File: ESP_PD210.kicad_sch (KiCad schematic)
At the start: 66 parts, among them J1 TTL, J2 CART, J3 USB_C_Receptacle_USB2.0, Q1 NPN, Q2 SE30P09D, SW1 Rocker, SW2 Move, U1 SSD1316, U2 ESP8684, U3 AD8628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

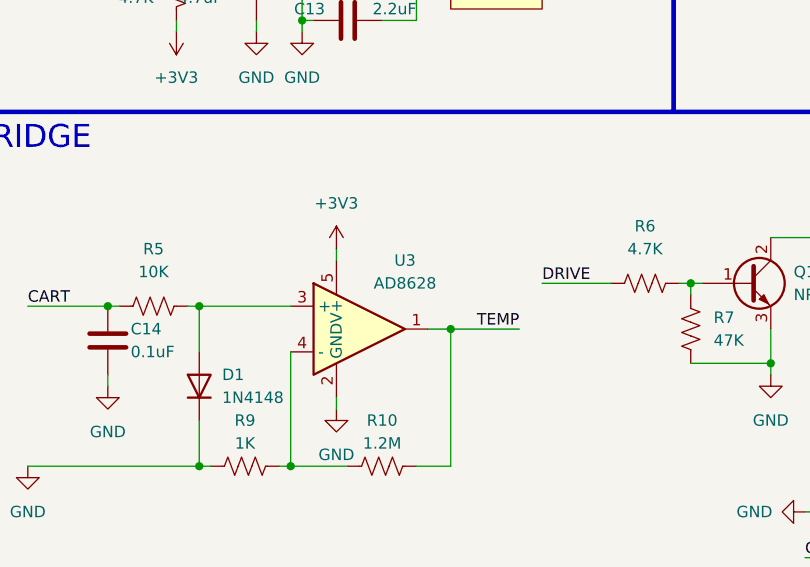
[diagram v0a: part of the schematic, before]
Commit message: Replace the OPA with OPA188
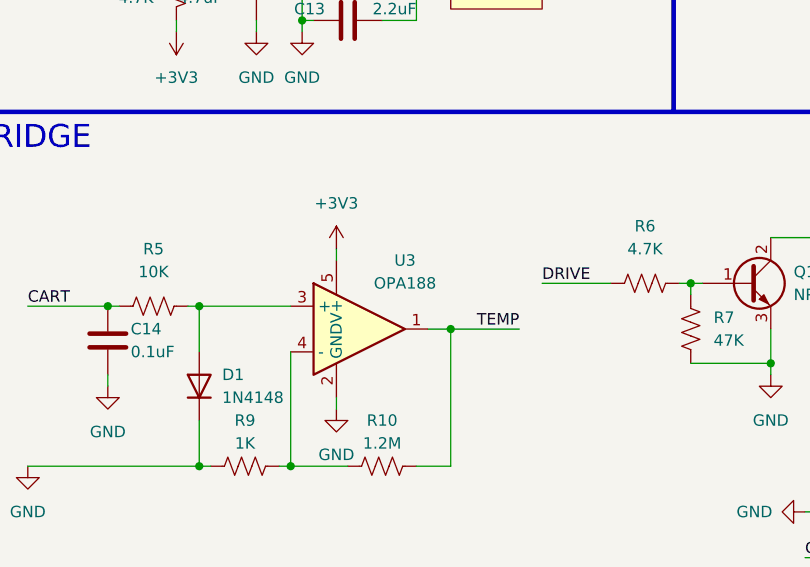
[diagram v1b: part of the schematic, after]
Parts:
- U3: value AD8628 -> OPA188
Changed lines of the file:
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@@
     (in_bom yes) (on_board yes)
     (property "Reference" "U3" (id 0) (at 193.04 82.55 0))
-    (property "Value" "AD8628" (id 1) (at 193.04 85.09 0))
+    (property "Value" "OPA188" (id 1) (at 193.04 85.09 0))
     (property "Footprint" "Package_TO_SOT_SMD:SOT-23-5" (id 2) (at 186.69 86.36 0)
       (effects (font (size 1.27 1.27)) hide)
@@
     )
     (path "/d2aeacdf-d9b9-4b18-ae2f-946cbfd5b011"
-      (reference "U3") (unit 1) (value "AD8628") (footprint "Package_TO_SOT_SMD:SOT-23-5")
+      (reference "U3") (unit 1) (value "OPA188") (footprint "Package_TO_SOT_SMD:SOT-23-5")
     )
     (path "/dade225f-9c7e-4650-bb58-a3ad4a9eac4c"

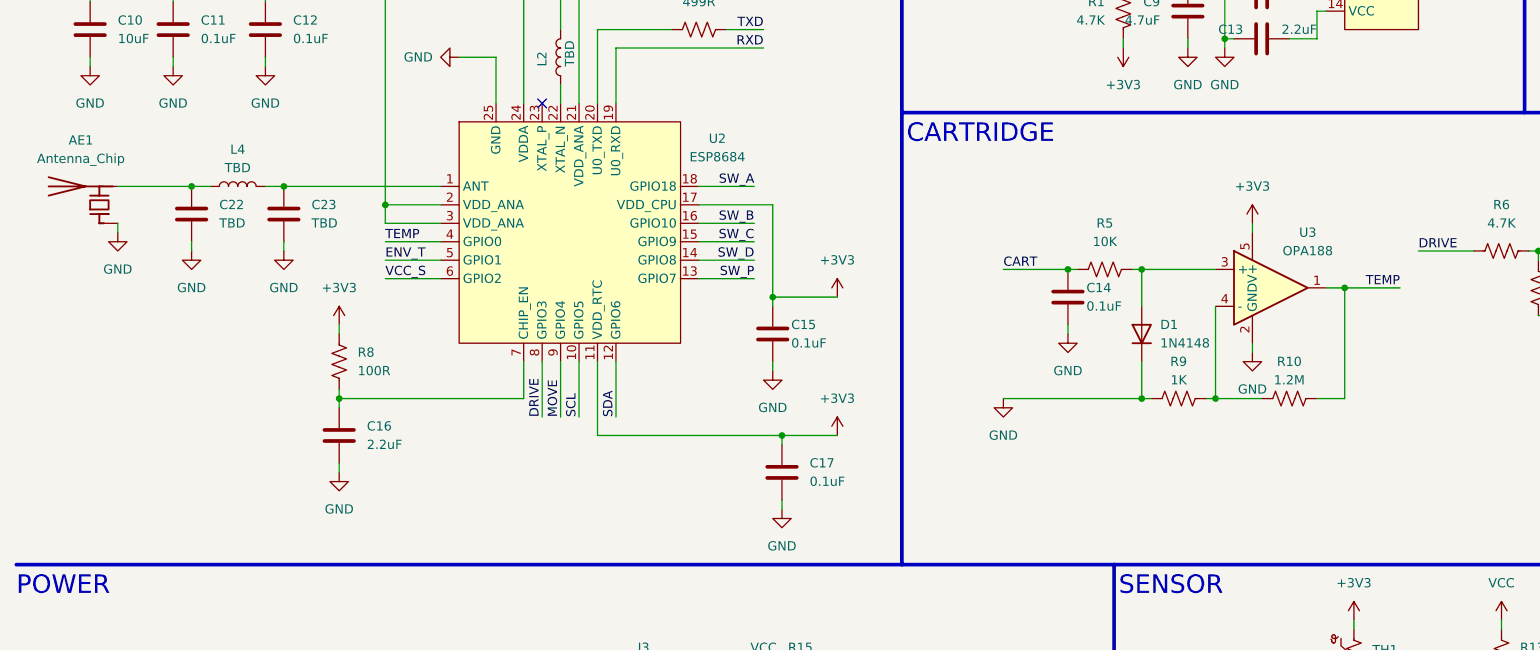
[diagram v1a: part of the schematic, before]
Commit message: 优化电源走线，增加 adc 处滤波电容
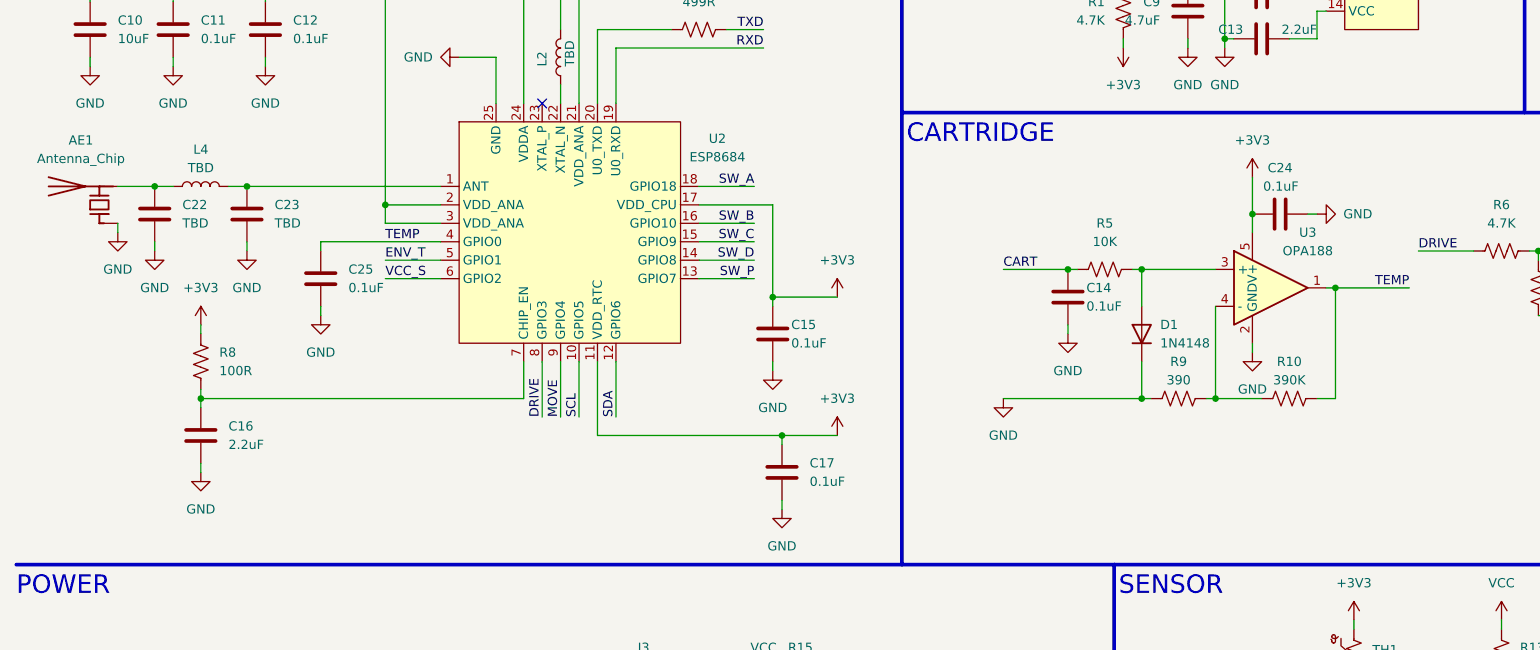
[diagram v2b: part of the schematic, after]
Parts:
- added C24, C25: 0.1uF, Capacitor_SMD:C_0402_1005Metric, symbol Device:C
- R10: value 1.2M -> 390K
- R9: value 1K -> 390
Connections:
- net +3V3: now also C24.1
- net GND: now also C24.2, C25.2
- net TEMP: now also C25.1
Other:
- moved on the sheet: C16, C22, C23, L4, R8
